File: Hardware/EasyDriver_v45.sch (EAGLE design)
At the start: 44 parts, among them IC1 A3967SLB, IC2 V_REG_317SMD

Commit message: Updating 2.4k to 2.49K resistor and updating to CC-SA 3.0
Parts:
- FRAME2: device SparkFun-Aesthetics:FRAME-LETTER -> SparkFun-Retired:FRAME-LETTER
- R5: value 2.4K -> 2.49K
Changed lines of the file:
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@@
 <part name="MOT_PWR" library="supply1" deviceset="V+" device=""/>
 <part name="GND1" library="supply1" deviceset="GND" device=""/>
-<part name="R5" library="SparkFun-Resistors" deviceset="RESISTOR" device="0603" value="2.4K"/>
+<part name="R5" library="SparkFun-Resistors" deviceset="RESISTOR" device="0603" value="2.49K"/>
 <part name="R6" library="SparkFun-Resistors" deviceset="RESISTOR" device="0603" value="390"/>
 <part name="R8" library="SparkFun-Resistors" deviceset="RESISTOR" device="0603" value="240"/>
@@
 <part name="GND8" library="supply1" deviceset="GND" device=""/>
 <part name="GND16" library="supply1" deviceset="GND" device=""/>
-<part name="FRAME2" library="SparkFun-Aesthetics" deviceset="FRAME-LETTER" device=""/>
+<part name="FRAME2" library="SparkFun-Retired" deviceset="FRAME-LETTER" device=""/>
 <part name="SUPPLY1" library="SparkFun-Aesthetics" deviceset="VCC" device=""/>
 <part name="SUPPLY2" library="SparkFun-Aesthetics" deviceset="VCC" device=""/>
@@
 <text x="116.84" y="154.94" size="1.778" layer="98">Max Coil Current(in Amps) = Vref(in Volts)/6</text>
 <text x="116.84" y="152.4" size="1.778" layer="98">Set R16 to 2.0V at factory = 333mA/phase</text>
-<rectangle x1="147.32" y1="22.86" x2="248.92" y2="35.56" layer="94"/>
 </plain>
 <instances>

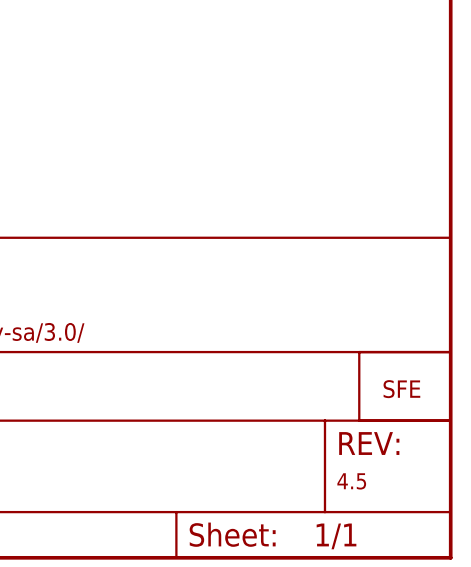
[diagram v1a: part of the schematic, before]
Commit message: added regular fiducials
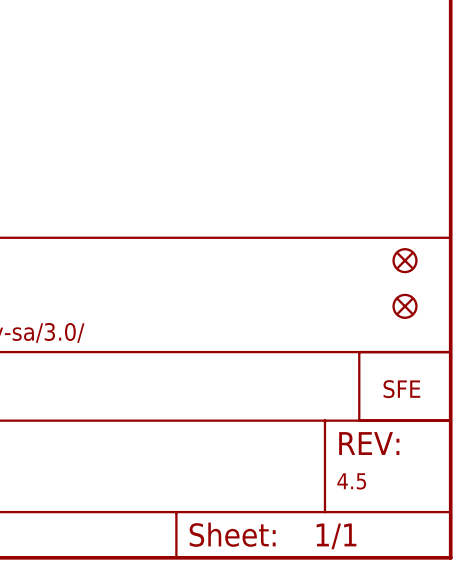
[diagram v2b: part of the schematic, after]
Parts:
- added FID1, FID2: FIDUCIAL1X2, SparkFun-Aesthetics:FIDUCIAL1X2
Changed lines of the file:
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@@
 <?xml version="1.0" encoding="utf-8"?>
 <!DOCTYPE eagle SYSTEM "eagle.dtd">
-<eagle version="6.5.0">
+<eagle version="6.6.0">
 <drawing>
 <settings>
@@
 <part name="SUPPLY4" library="SparkFun-Aesthetics" deviceset="VCC" device=""/>
 <part name="SUPPLY5" library="SparkFun-Aesthetics" deviceset="VCC" device=""/>
+<part name="FID1" library="SparkFun-Aesthetics" deviceset="FIDUCIAL" device="1X2"/>
+<part name="FID2" library="SparkFun-Aesthetics" deviceset="FIDUCIAL" device="1X2"/>
 </parts>
 <sheets>
@@
 </instance>
 <instance part="SUPPLY5" gate="G$1" x="114.3" y="104.14"/>
+<instance part="FID1" gate="G$1" x="243.84" y="33.02"/>
+<instance part="FID2" gate="G$1" x="243.84" y="27.94"/>
 </instances>
 <busses>

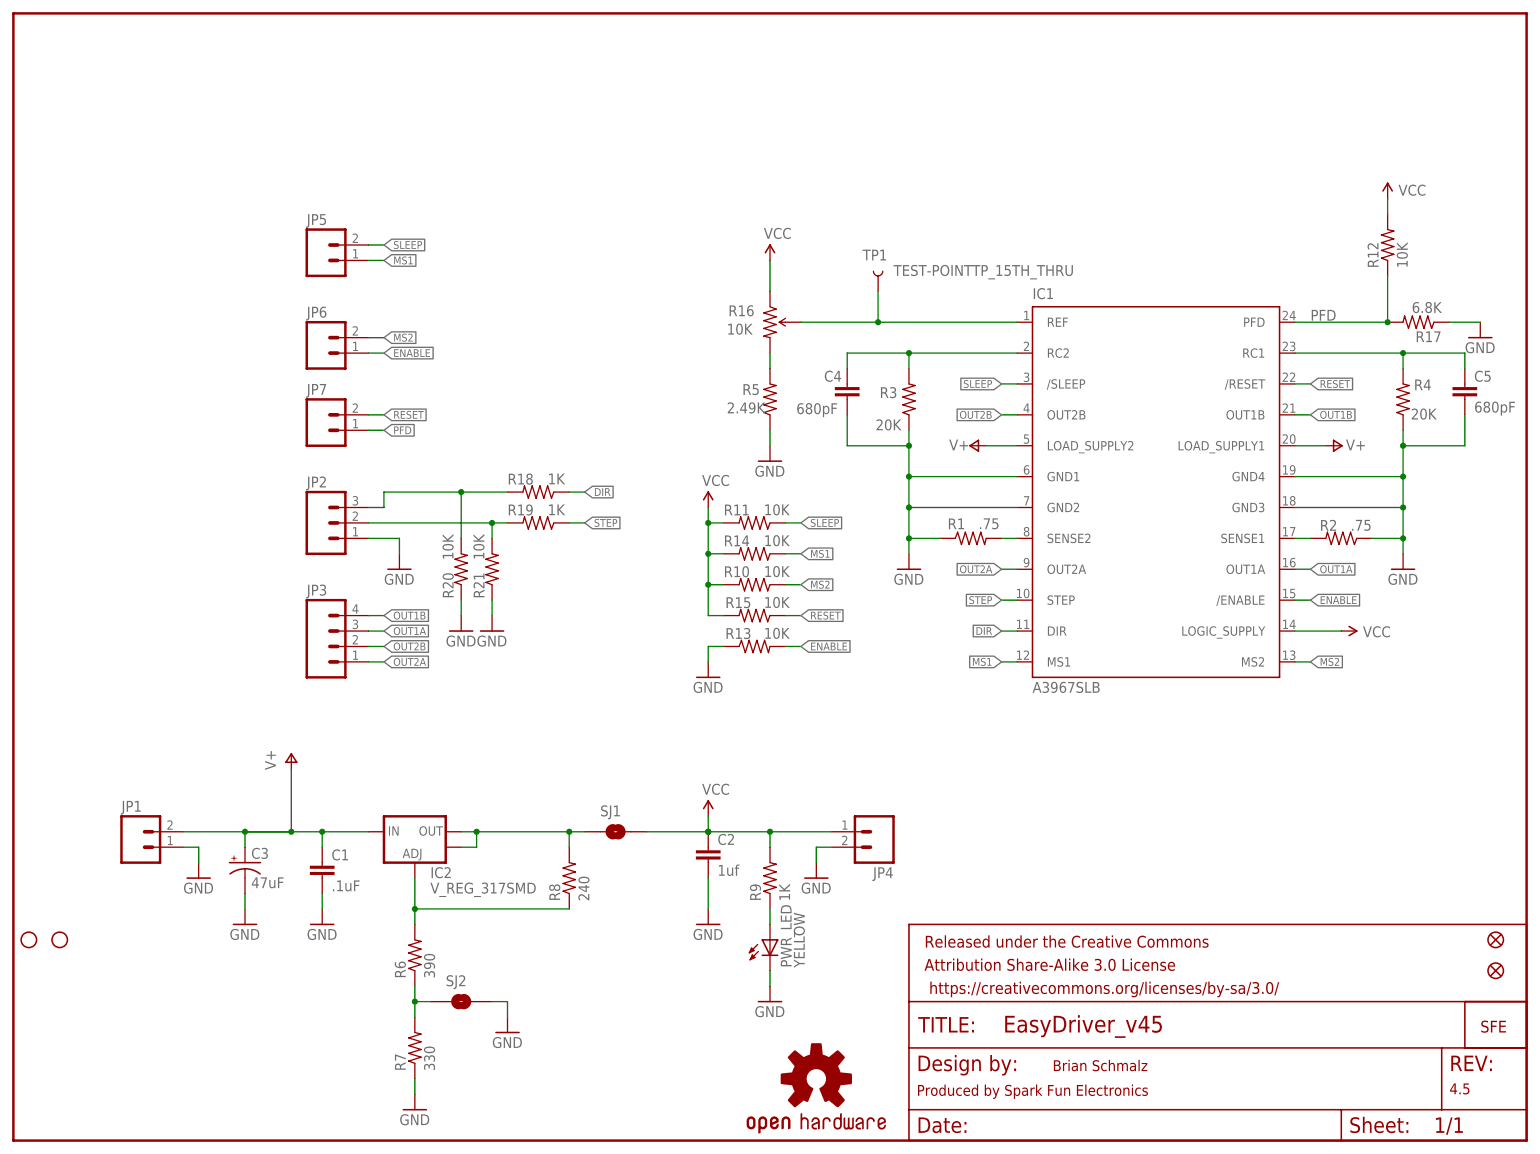
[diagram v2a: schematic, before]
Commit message: Minor edits to some of schematic guide text for clarity of function (SJ1 mainly). Created schematic PDF so we can link to it in GitHub.
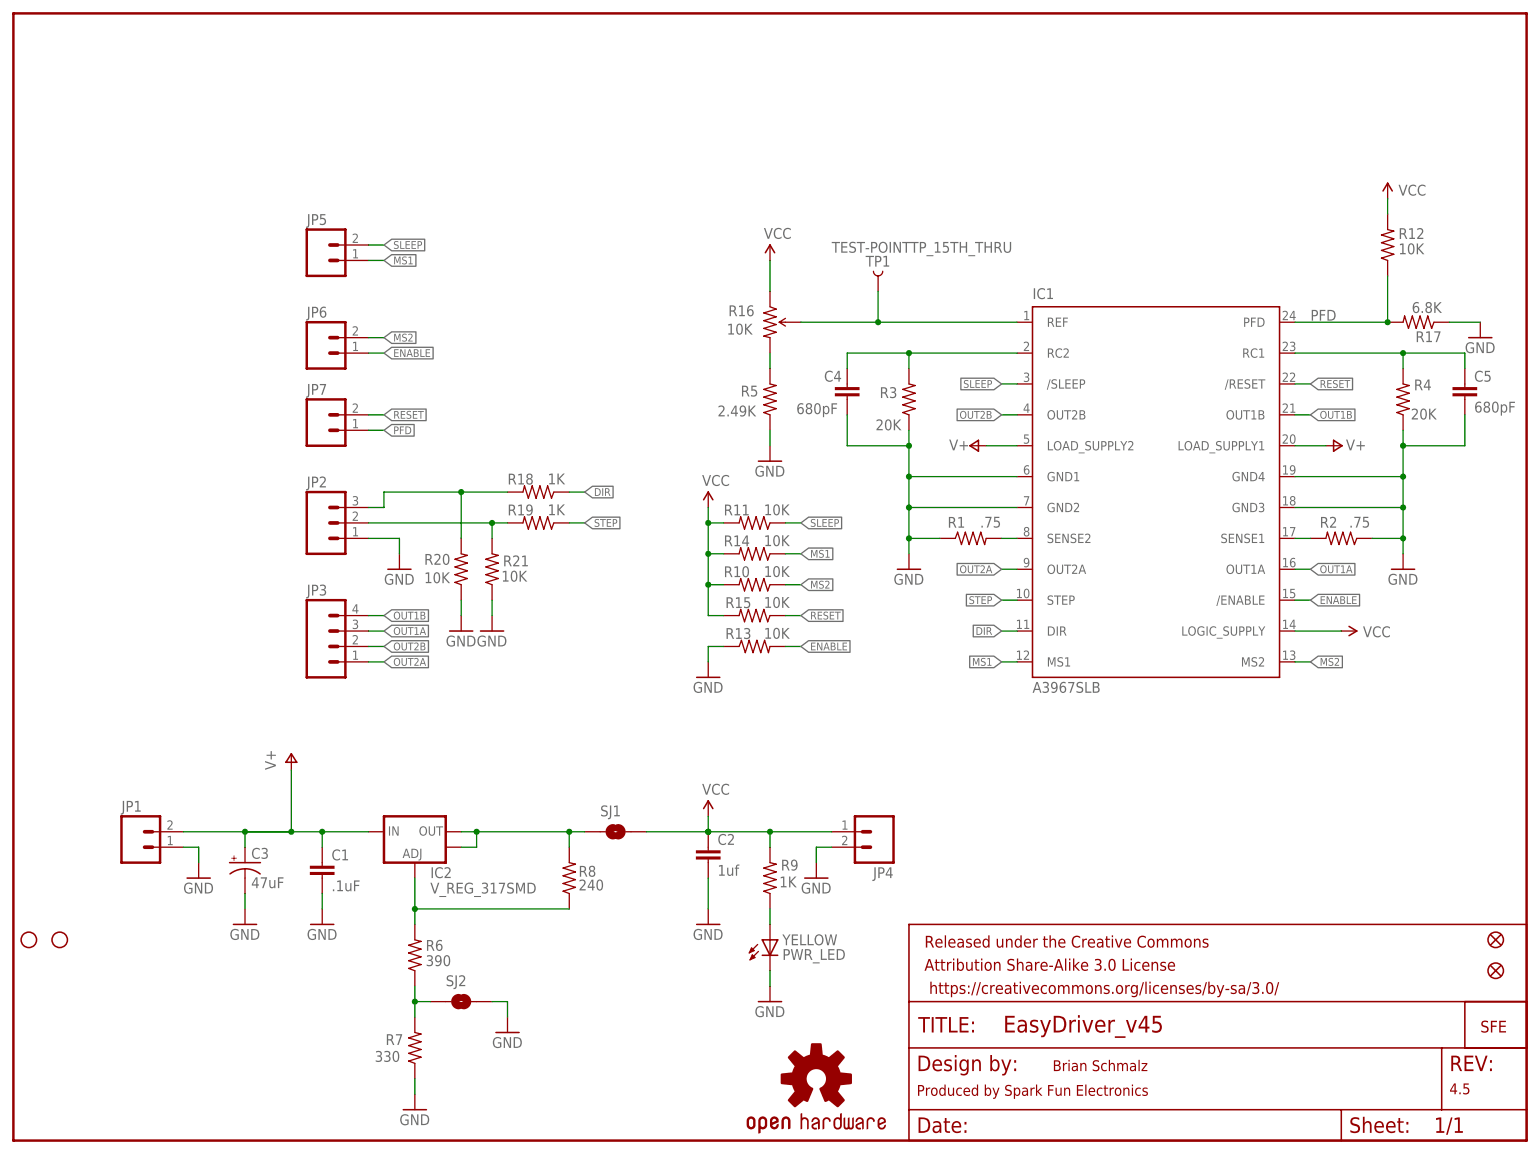
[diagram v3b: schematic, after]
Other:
- note added: "SJ1 (APWR) Shorted with copper trace from factory. Cut trace to disconnect IC2 power supply from Vcc and then supply your own Vcc (3.3V or 5V) to the "5V" pin."
- note added: "SJ2 (3/5V) Normally Open -> Vcc=5.0V Closed -> Vcc = 3.3V"
- note removed: "Cut to use your own"
- note removed: "SJ1 Normally Shorted"
- note removed: "SJ2 Closed -> Vcc = 3.3V"
- note removed: "SJ2 Normally Open -> Vcc=5.0V"
- note removed: "Vcc source from JP4"
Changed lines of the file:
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@@
 <?xml version="1.0" encoding="utf-8"?>
 <!DOCTYPE eagle SYSTEM "eagle.dtd">
-<eagle version="6.6.0">
+<eagle version="6.5.0">
 <drawing>
 <settings>
@@
 <text x="48.26" y="58.42" size="1.778" layer="98">Must use LM317</text>
 <text x="48.26" y="55.88" size="1.778" layer="98">For 30V V+ input</text>
-<text x="81.28" y="60.96" size="1.778" layer="98">SJ1 Normally Shorted</text>
-<text x="81.28" y="58.42" size="1.778" layer="98">Cut to use your own</text>
-<text x="81.28" y="55.88" size="1.778" layer="98">Vcc source from JP4</text>
+<text x="77.216" y="57.15" size="1.778" layer="98">SJ1 (APWR) Shorted with copper
+trace from factory. Cut trace to
+disconnect IC2 power supply
+from Vcc and then supply your
+own Vcc (3.3V or 5V) to the "5V"
+pin.</text>
 <text x="5.08" y="63.5" size="1.778" layer="98">Power Input</text>
 <text x="5.08" y="60.96" size="1.778" layer="98">8V to 30V (Vcc = 5V)</text>
 <text x="5.08" y="58.42" size="1.778" layer="98">6.3V to 30V (Vcc = 3.3V)</text>
-<text x="73.66" y="12.7" size="1.778" layer="98">SJ2 Normally Open -&gt; Vcc=5.0V</text>
-<text x="73.66" y="10.16" size="1.778" layer="98">SJ2 Closed -&gt; Vcc = 3.3V</text>
+<text x="77.47" y="21.59" size="1.778" layer="98">SJ2 (3/5V)
+   Normally Open -&gt; Vcc=5.0V
+   Closed -&gt; Vcc = 3.3V</text>
 <text x="116.84" y="177.8" size="1.778" layer="98">TP1 = Vref input to driver</text>
 <text x="116.84" y="175.26" size="1.778" layer="98">Monitor this test point with meter</text>
@@
 <instance part="GND6" gate="1" x="114.3" y="76.2"/>
 <instance part="R1" gate="G$1" x="157.48" y="99.06" smashed="yes">
-<attribute name="NAME" x="153.67" y="100.5586" size="1.778" layer="95"/>
-<attribute name="VALUE" x="158.75" y="100.584" size="1.778" layer="96"/>
+<attribute name="NAME" x="153.67" y="100.8126" size="1.778" layer="95"/>
+<attribute name="VALUE" x="159.004" y="100.838" size="1.778" layer="96"/>
 </instance>
 <instance part="R2" gate="G$1" x="218.44" y="99.06" smashed="yes" rot="R180">
-<attribute name="NAME" x="214.884" y="100.3046" size="1.778" layer="95"/>
-<attribute name="VALUE" x="219.964" y="100.33" size="1.778" layer="96"/>
+<attribute name="NAME" x="214.884" y="100.8126" size="1.778" layer="95"/>
+<attribute name="VALUE" x="219.71" y="100.838" size="1.778" layer="96"/>
 </instance>
 <instance part="R4" gate="G$1" x="228.6" y="121.92" smashed="yes" rot="R90">
@@
 <instance part="GND1" gate="1" x="124.46" y="111.76"/>
 <instance part="R5" gate="G$1" x="124.46" y="121.92" smashed="yes" rot="R90">
-<attribute name="NAME" x="119.888" y="122.6566" size="1.778" layer="95"/>
-<attribute name="VALUE" x="117.348" y="119.634" size="1.778" layer="96"/>
-</instance>
-<instance part="R6" gate="G$1" x="66.04" y="30.48" rot="R90"/>
-<instance part="R8" gate="G$1" x="91.44" y="43.18" rot="R90"/>
-<instance part="PWR_LED" gate="G$1" x="124.46" y="33.02"/>
-<instance part="R9" gate="G$1" x="124.46" y="43.18" rot="R90"/>
+<attribute name="NAME" x="119.634" y="122.4026" size="1.778" layer="95"/>
+<attribute name="VALUE" x="115.824" y="119.126" size="1.778" layer="96"/>
+</instance>
+<instance part="R6" gate="G$1" x="66.04" y="30.48" smashed="yes" rot="R90">
+<attribute name="NAME" x="67.818" y="31.2166" size="1.778" layer="95"/>
+<attribute name="VALUE" x="67.818" y="28.702" size="1.778" layer="96"/>
+</instance>
+<instance part="R8" gate="G$1" x="91.44" y="43.18" smashed="yes" rot="R90">
+<attribute name="NAME" x="92.964" y="43.4086" size="1.778" layer="95"/>
+<attribute name="VALUE" x="92.964" y="41.148" size="1.778" layer="96"/>
+</instance>
+<instance part="PWR_LED" gate="G$1" x="124.46" y="33.02" smashed="yes">
+<attribute name="NAME" x="126.492" y="29.718" size="1.778" layer="95"/>
+<attribute name="VALUE" x="126.492" y="32.131" size="1.778" layer="96"/>
+</instance>
+<instance part="R9" gate="G$1" x="124.46" y="43.18" smashed="yes" rot="R90">
+<attribute name="NAME" x="126.238" y="44.4246" size="1.778" layer="95"/>
+<attribute name="VALUE" x="125.984" y="41.656" size="1.778" layer="96"/>
+</instance>
 <instance part="R11" gate="G$1" x="121.92" y="101.6" smashed="yes" rot="R180">
 <attribute name="NAME" x="116.84" y="102.8446" size="1.778" layer="95"/>
 <attribute name="VALUE" x="123.444" y="102.87" size="1.778" layer="96"/>
 </instance>
-<instance part="R12" gate="G$1" x="226.06" y="147.32" rot="R90"/>
+<instance part="R12" gate="G$1" x="226.06" y="147.32" smashed="yes" rot="R90">
+<attribute name="NAME" x="227.838" y="148.3106" size="1.778" layer="95"/>
+<attribute name="VALUE" x="227.838" y="145.796" size="1.778" layer="96"/>
+</instance>
 <instance part="R13" gate="G$1" x="121.92" y="81.28" smashed="yes">
 <attribute name="NAME" x="117.094" y="82.5246" size="1.778" layer="95"/>
@@
 <instance part="SJ1" gate="1" x="99.06" y="50.8"/>
 <instance part="SJ2" gate="1" x="73.66" y="22.86"/>
-<instance part="R7" gate="G$1" x="66.04" y="15.24" rot="R90"/>
+<instance part="R7" gate="G$1" x="66.04" y="15.24" smashed="yes" rot="R90">
+<attribute name="NAME" x="61.214" y="15.7226" size="1.778" layer="95"/>
+<attribute name="VALUE" x="59.436" y="12.954" size="1.778" layer="96"/>
+</instance>
 <instance part="R16" gate="R?" x="124.46" y="134.62" smashed="yes" rot="R270">
 <attribute name="NAME" x="117.602" y="135.6106" size="1.778" layer="95"/>
@@
 <instance part="GND7" gate="1" x="63.5" y="93.98"/>
 <instance part="R20" gate="G$1" x="73.66" y="93.98" smashed="yes" rot="R90">
-<attribute name="NAME" x="72.4154" y="89.154" size="1.778" layer="95" rot="R90"/>
-<attribute name="VALUE" x="72.39" y="95.504" size="1.778" layer="96" rot="R90"/>
+<attribute name="NAME" x="67.564" y="94.7166" size="1.778" layer="95"/>
+<attribute name="VALUE" x="67.564" y="91.694" size="1.778" layer="96"/>
 </instance>
 <instance part="R21" gate="G$1" x="78.74" y="93.98" smashed="yes" rot="R90">
-<attribute name="NAME" x="77.4954" y="89.154" size="1.778" layer="95" rot="R90"/>
-<attribute name="VALUE" x="77.47" y="95.504" size="1.778" layer="96" rot="R90"/>
+<attribute name="NAME" x="80.518" y="94.4626" size="1.778" layer="95"/>
+<attribute name="VALUE" x="80.264" y="91.948" size="1.778" layer="96"/>
 </instance>
 <instance part="TP1" gate="G$1" x="142.24" y="139.7" smashed="yes" rot="R90">
-<attribute name="NAME" x="139.7" y="144.78" size="1.778" layer="95"/>
-<attribute name="VALUE" x="144.78" y="142.24" size="1.778" layer="96"/>
+<attribute name="NAME" x="140.208" y="143.764" size="1.778" layer="95"/>
+<attribute name="VALUE" x="134.62" y="146.05" size="1.778" layer="96"/>
 </instance>
 <instance part="GND8" gate="1" x="73.66" y="83.82"/>
